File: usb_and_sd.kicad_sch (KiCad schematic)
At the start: 77 parts, among them J7001 USB_C_Receptacle_USB2.0_16P, J7002 USB_A, J7003 Micro_SD_Card_Det1, U1001 AM6231ASGGGAALW, U7001 TVS0500DRVR, U7002 EMMC16G-TB29-PZ90, U7004 TPD3S014, U7005 TPS22918DBVR

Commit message: Labeled all nets and added some footprints
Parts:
- U1001: footprint (none) -> AM6231ASGGGAALW:BGA425C50P25X25_1300X1300X89
- U7002: footprint (none) -> Package_BGA:LFBGA-153_11.5x13mm_Layout14x14_P0.5mm
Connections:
- net USB_C_DM is gone; now on net USB_C_DN: D7002.2 (A2), J7001.A7 (D-), J7001.B7 (D-), L7001.2
- net USB_C_DN: no longer D7001.2 (A2), J7001.A6 (D+), J7001.B6 (D+), L7001.3
- net USB1_DP: now reaches L7002.1, U1001.AE9 (USB1_DP)
- net USB_A_DP: now reaches J7002.3 (D+), L7002.2, U7004.5 (D1)
- net USB_A_DN: now reaches J7002.2 (D-), L7002.3, U7004.6 (D2)
- net USB1_DN: now reaches L7002.4, U1001.AD10 (USB1_DM)
- net USB0_VBUS: now reaches R7002.2, R7003.1, U1001.AC11 (USB0_VBUS)
- net USB0_DN: now reaches L7001.1, U1001.AE11 (USB0_DM)
- net USB0_DP: now reaches L7001.4, U1001.AD11 (USB0_DP)
- net SD_LS_ON: now reaches D7013.2 (A), D7014.2 (A), R7031.2, U7005.3 (ON)
- net USB_A_LS_EN: now reaches C7016.1, R7023.2, U7004.1 (EN)
- net EMMC_RSTn: now reaches D7003.2 (A), D7004.2 (A), D7005.2 (A), R7013.2, U7002.K5 (RST_n)
- net EMMC_VDDI: now reaches C7014.1, U7002.C2 (VDDI)
- net EMMC_DS: now reaches R7020.2, U7002.H5 (DS)
- net USB0_RCALIB: now reaches R7015.2, U1001.AE10 (USB0_RCALIB)
- net USB0_RCALIB: now also R7018.2, U1001.AC9 (USB1_RCALIB)
- net USB_A_VBUS: now reaches C7017.1, J7002.1 (VBUS), R7021.2, U7004.4 (OUT)
- net USB_C_CC2: now reaches J7001.B5 (CC2), R7017.1
- net USB_C_CC1: now reaches J7001.A5 (CC1), R7016.1
- net USB1_VBUS: now reaches R7021.1, R7022.2, U1001.AB10 (USB1_VBUS)
- net USB1_DRVVBUS: now reaches R7023.1, U1001.F18 (USB1_DRVVBUS)
- new net USB_C_DP: D7001.2 (A2), J7001.A6 (D+), J7001.B6 (D+), L7001.3
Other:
- moved on the sheet: R7002, R7003, R7018, R7019, R7020

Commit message: Added some footprints for important ICs
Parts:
- J7001: footprint (none) -> Connector_USB:USB_C_Receptacle_HRO_TYPE-C-31-M-12
- J7002: footprint (none) -> Connector_USB:USB_A_Molex_48037-2200_Horizontal
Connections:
- net EMMC_RSTn renamed EMMC_RST_N
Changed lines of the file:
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@@
 		)
 	)
-	(label "EMMC_RSTn"
+	(label "EMMC_RST_N"
 		(at 547.37 189.23 0)
 		(effects
@@
 			)
 		)
-		(property "Footprint" ""
+		(property "Footprint" "Connector_USB:USB_A_Molex_48037-2200_Horizontal"
 			(at 234.95 195.58 0)
 			(effects
@@
 			)
 		)
-		(property "Footprint" ""
+		(property "Footprint" "Connector_USB:USB_C_Receptacle_HRO_TYPE-C-31-M-12"
 			(at 236.22 147.32 0)
 			(effects

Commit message: Added more IC footprints
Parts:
- L7001, L7002: footprint (none) -> SoftServicesFootprintLibrary:SRF2012-900YA
- U7005: footprint (none) -> TPS22918DBVR:SOT95P280X145-6N
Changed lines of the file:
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@@
 			)
 		)
-		(property "Footprint" ""
+		(property "Footprint" "SoftServicesFootprintLibrary:SRF2012-900YA"
 			(at 163.83 194.31 0)
 			(effects
@@
 			)
 		)
-		(property "Footprint" ""
+		(property "Footprint" "SoftServicesFootprintLibrary:SRF2012-900YA"
 			(at 142.24 147.32 0)
 			(effects
@@
 			)
 		)
-		(property "Footprint" ""
+		(property "Footprint" "TPS22918DBVR:SOT95P280X145-6N"
 			(at 598.17 378.46 0)
 			(effects

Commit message: Added more footprints
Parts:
- U7001: footprint (none) -> Package_SON:WSON-6-1EP_2x2mm_P0.65mm_EP1x1.6mm
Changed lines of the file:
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@@
 			)
 		)
-		(property "Footprint" ""
+		(property "Footprint" "Package_SON:WSON-6-1EP_2x2mm_P0.65mm_EP1x1.6mm"
 			(at 165.1 120.65 0)
 			(effects

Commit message: Added many more footprints
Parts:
- J7003: footprint (none) -> TF-15x15:TF15X15
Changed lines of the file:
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@@
 			)
 		)
-		(property "Footprint" ""
+		(property "Footprint" "TF-15x15:TF15X15"
 			(at 703.58 284.48 0)
 			(effects

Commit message: Double checked power, ddr4, USB, MMC and added bootstrap. Also added buttons and added pinmuxing in sysconfig
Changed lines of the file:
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@@
 	)
 	(junction
+		(at 561.34 179.07)
+		(diameter 0)
+		(color 0 0 0 0)
+	)
+	(junction
 		(at 520.7 161.29)
 		(diameter 0)
@@
 	(wire
 		(pts
+			(xy 547.37 179.07) (xy 561.34 179.07)
+		)
+		(stroke
+			(width 0)
+			(type default)
+		)
+	)
+	(wire
+		(pts
 			(xy 551.18 322.58) (xy 551.18 325.12)
 		)
@@
 	)
 	(label "EMMC_CLK"
-		(at 561.34 179.07 0)
+		(at 547.37 179.07 0)
 		(effects
 			(font

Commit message: Added almost all passive component footprints
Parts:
- C7001, C7011, C7018: footprint (none) -> Capacitor_SMD:C_0402_1005Metric
- C7002, C7003, C7004, C7005, C7006, C7007, C7008, C7009, C7010, C7013, C7014, C7016, C7019, C7020: footprint (none) -> Capacitor_SMD:C_0201_0603Metric
- C7012, C7015: footprint (none) -> Capacitor_SMD:C_0603_1608Metric
- C7017: footprint (none) -> Capacitor_SMD:C_1206_3216Metric
- C7021, C7022: footprint (none) -> Capacitor_SMD:C_0805_2012Metric
- D7001, D7002, D7006, D7007, D7008, D7009, D7010, D7011, D7012: footprint (none) -> Diode_SMD:D_SOD-882
- D7003, D7004, D7005, D7013, D7014: footprint (none) -> Diode_SMD:D_SOD-523
- R7001, R7014: footprint (none) -> Resistor_SMD:R_0201_0603Metric
- R7002, R7003, R7004, R7005, R7006, R7007, R7008, R7009, R7010, R7011, R7012, R7013, R7015, R7016, R7017, R7018, R7019, R7020, R7021, R7022, R7023, R7024, R7025, R7026, R7027, R7028, R7029, R7030, R7031: footprint (none) -> Resistor_SMD:R_0402_1005Metric
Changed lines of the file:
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@@
 			)
 		)
-		(property "Footprint" ""
+		(property "Footprint" "Resistor_SMD:R_0402_1005Metric"
 			(at 498.602 139.7 90)
 			(effects
@@
 			)
 		)
-		(property "Footprint" ""
+		(property "Footprint" "Resistor_SMD:R_0402_1005Metric"
 			(at 118.11 133.858 90)
 			(effects
@@
 			)
 		)
-		(property "Footprint" ""
+		(property "Footprint" "Diode_SMD:D_SOD-523"
 			(at 548.64 378.46 0)
 			(effects
@@
 			)
 		)
-		(property "Footprint" ""
+		(property "Footprint" "Capacitor_SMD:C_0201_0603Metric"
 			(at 586.4352 322.58 0)
 			(effects
@@
 			)
 		)
-		(property "Footprint" ""
+		(property "Footprint" "Resistor_SMD:R_0201_0603Metric"
 			(at 415.29 151.638 90)
 			(effects
@@
 			)
 		)
-		(property "Footprint" ""
+		(property "Footprint" "Diode_SMD:D_SOD-882"
 			(at 184.15 161.29 0)
 			(effects
@@
 			)
 		)
-		(property "Footprint" ""
+		(property "Footprint" "Capacitor_SMD:C_0805_2012Metric"
 			(at 616.9152 391.16 0)
 			(effects
@@
 			)
 		)
-		(property "Footprint" ""
+		(property "Footprint" "Capacitor_SMD:C_0201_0603Metric"
 			(at 172.4152 264.16 0)
 			(effects
@@
 			)
 		)
-		(property "Footprint" ""
+		(property "Footprint" "Resistor_SMD:R_0402_1005Metric"
 			(at 488.442 139.7 90)
 			(effects
@@
 			)
 		)
-		(property "Footprint" ""
+		(property "Footprint" "Diode_SMD:D_SOD-523"
 			(at 520.7 200.66 0)
 			(effects
@@
 			)
 		)
-		(property "Footprint" ""
+		(property "Footprint" "Resistor_SMD:R_0402_1005Metric"
 			(at 539.242 139.7 90)
 			(effects
@@
 			)
 		)
-		(property "Footprint" ""
+		(property "Footprint" "Diode_SMD:D_SOD-523"
 			(at 520.7 195.58 0)
 			(effects
@@
 			)
 		)
-		(property "Footprint" ""
+		(property "Footprint" "Resistor_SMD:R_0201_0603Metric"
 			(at 415.29 121.158 90)
 			(effects
@@
 			)
 		)
-		(property "Footprint" ""
+		(property "Footprint" "Resistor_SMD:R_0402_1005Metric"
 			(at 549.402 139.7 90)
 			(effects
@@
 			)
 		)
-		(property "Footprint" ""
+		(property "Footprint" "Capacitor_SMD:C_0402_1005Metric"
 			(at 544.5252 120.65 0)
 			(effects
@@
 			)
 		)
-		(property "Footprint" ""
+		(property "Footprint" "Diode_SMD:D_SOD-882"
 			(at 561.34 318.77 0)
 			(effects
@@
 			)
 		)
-		(property "Footprint" ""
+		(property "Footprint" "Capacitor_SMD:C_0201_0603Metric"
 			(at 643.5852 120.65 0)
 			(effects
@@
 			)
 		)
-		(property "Footprint" ""
+		(property "Footprint" "Resistor_SMD:R_0402_1005Metric"
 			(at 579.882 139.7 90)
 			(effects
@@
 			)
 		)
-		(property "Footprint" ""
+		(property "Footprint" "Diode_SMD:D_SOD-882"
 			(at 530.86 318.77 0)
 			(effects
@@
 			)
 		)
-		(property "Footprint" ""
+		(property "Footprint" "Resistor_SMD:R_0402_1005Metric"
 			(at 573.278 198.12 90)
 			(effects
@@
 			)
 		)
-		(property "Footprint" ""
+		(property "Footprint" "Capacitor_SMD:C_0201_0603Metric"
 			(at 599.1352 322.58 0)
 			(effects
@@
 			)
 		)
-		(property "Footprint" ""
+		(property "Footprint" "Resistor_SMD:R_0402_1005Metric"
 			(at 621.792 284.48 90)
 			(effects
@@
 			)
 		)
-		(property "Footprint" ""
+		(property "Footprint" "Diode_SMD:D_SOD-882"
 			(at 172.72 161.29 0)
 			(effects
@@
 			)
 		)
-		(property "Footprint" ""
+		(property "Footprint" "Capacitor_SMD:C_0402_1005Metric"
 			(at 707.0852 120.65 0)
 			(effects
@@
 			)
 		)
-		(property "Footprint" ""
+		(property "Footprint" "Capacitor_SMD:C_0201_0603Metric"
 			(at 557.2252 120.65 0)
 			(effects
@@
 			)
 		)
-		(property "Footprint" ""
+		(property "Footprint" "Resistor_SMD:R_0402_1005Metric"
 			(at 558.292 370.84 90)
 			(effects
@@
 			)
 		)
-		(property "Footprint" ""
+		(property "Footprint" "Diode_SMD:D_SOD-882"
 			(at 623.57 321.31 0)
 			(effects
@@
 			)
 		)
-		(property "Footprint" ""
+		(property "Footprint" "Resistor_SMD:R_0402_1005Metric"
 			(at 122.428 161.29 90)
 			(effects
@@
 			)
 		)
-		(property "Footprint" ""
+		(property "Footprint" "Resistor_SMD:R_0402_1005Metric"
 			(at 205.232 161.29 90)
 			(effects
@@
 			)
 		)
-		(property "Footprint" ""
+		(property "Footprint" "Resistor_SMD:R_0402_1005Metric"
 			(at 104.14 170.942 90)
 			(effects
@@
 			)
 		)
-		(property "Footprint" ""
+		(property "Footprint" "Resistor_SMD:R_0402_1005Metric"
 			(at 518.922 284.48 90)
 			(effects
@@
 			)
 		)
-		(property "Footprint" ""
+		(property "Footprint" "Diode_SMD:D_SOD-882"
 			(at 551.18 318.77 0)
 			(effects
@@
 			)
 		)
-		(property "Footprint" ""
+		(property "Footprint" "Resistor_SMD:R_0402_1005Metric"
 			(at 563.118 198.12 90)
 			(effects
@@
 			)
 		)
-		(property "Footprint" ""
+		(property "Footprint" "Resistor_SMD:R_0402_1005Metric"
 			(at 508.762 284.48 90)
 			(effects
@@
 			)
 		)
-		(property "Footprint" ""
+		(property "Footprint" "Capacitor_SMD:C_0201_0603Metric"
 			(at 694.3852 120.65 0)
 			(effects
@@
 			)
 		)
-		(property "Footprint" ""
+		(property "Footprint" "Diode_SMD:D_SOD-882"
 			(at 541.02 318.77 0)
 			(effects
@@
 			)
 		)
-		(property "Footprint" ""
+		(property "Footprint" "Resistor_SMD:R_0402_1005Metric"
 			(at 529.082 139.7 90)
 			(effects
@@
 			)
 		)
-		(property "Footprint" ""
+		(property "Footprint" "Resistor_SMD:R_0402_1005Metric"
 			(at 127.508 219.71 90)
 			(effects
@@
 			)
 		)
-		(property "Footprint" ""
+		(property "Footprint" "Capacitor_SMD:C_0201_0603Metric"
 			(at 569.9252 120.65 0)
 			(effects
@@
 			)
 		)
-		(property "Footprint" ""
+		(property "Footprint" "Resistor_SMD:R_0402_1005Metric"
 			(at 569.722 139.7 90)
 			(effects
@@
 			)
 		)
-		(property "Footprint" ""
+		(property "Footprint" "Capacitor_SMD:C_0805_2012Metric"
 			(at 577.5452 391.16 0)
 			(effects
@@
 			)
 		)
-		(property "Footprint" ""
+		(property "Footprint" "Diode_SMD:D_SOD-882"
 			(at 520.7 318.77 0)
 			(effects
@@
 			)
 		)
-		(property "Footprint" ""
+		(property "Footprint" "Capacitor_SMD:C_0603_1608Metric"
 			(at 158.4452 264.16 0)
 			(effects
@@
 			)
 		)
-		(property "Footprint" ""
+		(property "Footprint" "Capacitor_SMD:C_0201_0603Metric"
 			(at 656.2852 120.65 0)
 			(effects
@@
 			)
 		)
-		(property "Footprint" ""
+		(property "Footprint" "Resistor_SMD:R_0402_1005Metric"
 			(at 518.922 139.7 90)
 			(effects
@@
 			)
 		)
-		(property "Footprint" ""
+		(property "Footprint" "Diode_SMD:D_SOD-523"
 			(at 520.7 205.74 0)
 			(effects
@@
 			)
 		)
-		(property "Footprint" ""
+		(property "Footprint" "Capacitor_SMD:C_0201_0603Metric"
 			(at 661.3652 189.23 0)
 			(effects
@@
 			)
 		)
-		(property "Footprint" ""
+		(property "Footprint" "Resistor_SMD:R_0402_1005Metric"
 			(at 508.762 139.7 90)
 			(effects
@@
 			)
 		)
-		(property "Footprint" ""
+		(property "Footprint" "Resistor_SMD:R_0402_1005Metric"
 			(at 559.562 139.7 90)
 			(effects
@@
 			)
 		)
-		(property "Footprint" ""
+		(property "Footprint" "Capacitor_SMD:C_0201_0603Metric"
 			(at 204.1652 128.27 0)
 			(effects
@@
 			)
 		)
-		(property "Footprint" ""
+		(property "Footprint" "Resistor_SMD:R_0402_1005Metric"
 			(at 102.87 133.858 90)
 			(effects
@@
 			)
 		)
-		(property "Footprint" ""
+		(property "Footprint" "Resistor_SMD:R_0402_1005Metric"
 			(at 137.16 253.238 90)
 			(effects
@@
 			)
 		)
-		(property "Footprint" ""
+		(property "Footprint" "Diode_SMD:D_SOD-882"
 			(at 510.54 318.77 0)
 			(effects
@@
 			)
 		)
-		(property "Footprint" ""
+		(property "Footprint" "Capacitor_SMD:C_0402_1005Metric"
 			(at 575.0052 322.58 0)
 			(effects
@@
 			)
 		)
-		(property "Footprint" ""
+		(property "Footprint" "Capacitor_SMD:C_0603_1608Metric"
 			(at 191.4652 128.27 0)
 			(effects
@@
 			)
 		)
-		(property "Footprint" ""
+		(property "Footprint" "Resistor_SMD:R_0402_1005Metric"
 			(at 193.802 161.29 90)
 			(effects
@@
 			)
 		)
-		(property "Footprint" ""
+		(property "Footprint" "Capacitor_SMD:C_0201_0603Metric"
 			(at 668.9852 120.65 0)
 			(effects
@@
 			)
 		)
-		(property "Footprint" ""
+		(property "Footprint" "Resistor_SMD:R_0402_1005Metric"
 			(at 559.562 284.48 90)
 			(effects
@@
 			)
 		)
-		(property "Footprint" ""
+		(property "Footprint" "Capacitor_SMD:C_0201_0603Metric"
 			(at 582.6252 120.65 0)
 			(effects
@@
 			)
 		)
-		(property "Footprint" ""
+		(property "Footprint" "Resistor_SMD:R_0402_1005Metric"
 			(at 529.082 284.48 90)
 			(effects
@@
 			)
 		)
-		(property "Footprint" ""
+		(property "Footprint" "Diode_SMD:D_SOD-523"
 			(at 548.64 383.54 0)
 			(effects
@@
 			)
 		)
-		(property "Footprint" ""
+		(property "Footprint" "Capacitor_SMD:C_0201_0603Metric"
 			(at 681.6852 120.65 0)
 			(effects
@@
 			)
 		)
-		(property "Footprint" ""
+		(property "Footprint" "Capacitor_SMD:C_1206_3216Metric"
 			(at 214.3252 264.16 0)
 			(effects
@@
 			)
 		)
-		(property "Footprint" ""
+		(property "Footprint" "Resistor_SMD:R_0402_1005Metric"
 			(at 137.16 213.868 90)
 			(effects
@@
 			)
 		)
-		(property "Footprint" ""
+		(property "Footprint" "Resistor_SMD:R_0402_1005Metric"
 			(at 549.402 284.48 90)
 			(effects
@@
 			)
 		)
-		(property "Footprint" ""
+		(property "Footprint" "Resistor_SMD:R_0402_1005Metric"
 			(at 539.242 284.48 90)
 			(effects
@@
 			)
 		)
-		(property "Footprint" ""
+		(property "Footprint" "Capacitor_SMD:C_0201_0603Metric"
 			(at 595.3252 120.65 0)
 			(effects

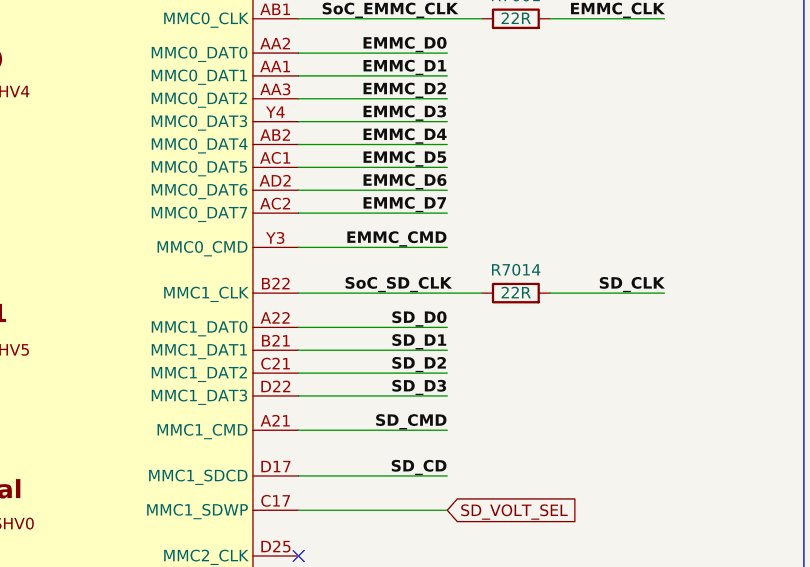
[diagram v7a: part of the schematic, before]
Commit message: Added net classes and colouring on layout editor
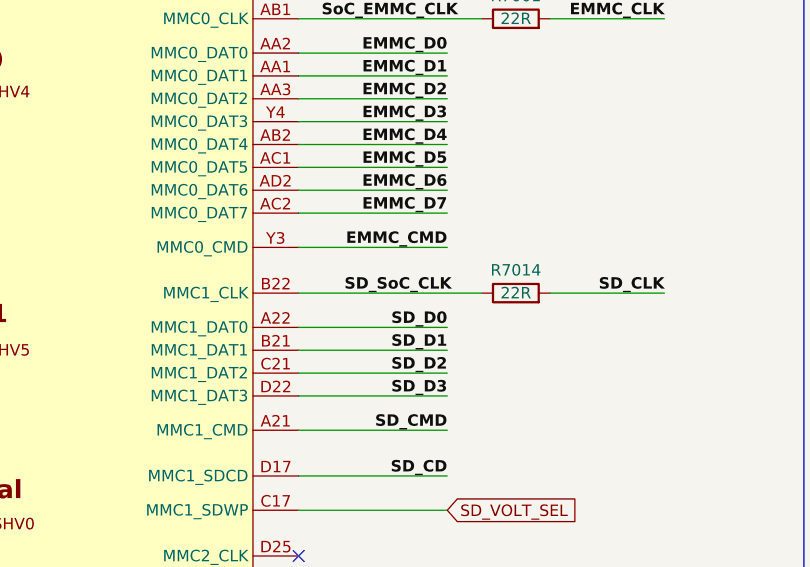
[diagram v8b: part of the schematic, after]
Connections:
- net SoC_SD_CLK renamed SD_SoC_CLK
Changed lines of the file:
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@@
 		)
 	)
-	(label "SoC_SD_CLK"
+	(label "SD_SoC_CLK"
 		(at 396.24 149.86 0)
 		(effects
